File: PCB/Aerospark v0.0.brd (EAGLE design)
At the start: 59.1 x 42.9 mm, 34 parts, among them U1 TMP102

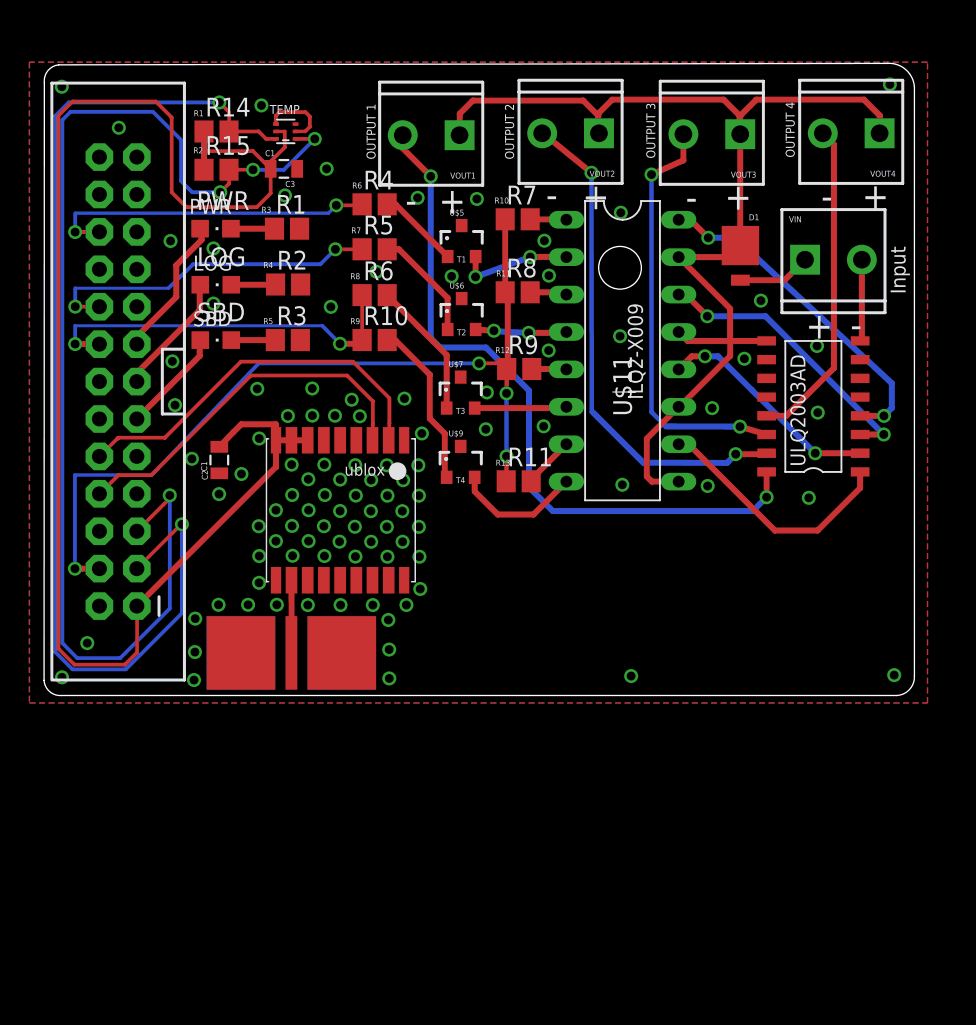
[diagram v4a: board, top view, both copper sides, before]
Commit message: Updated PCB and added mounting hole
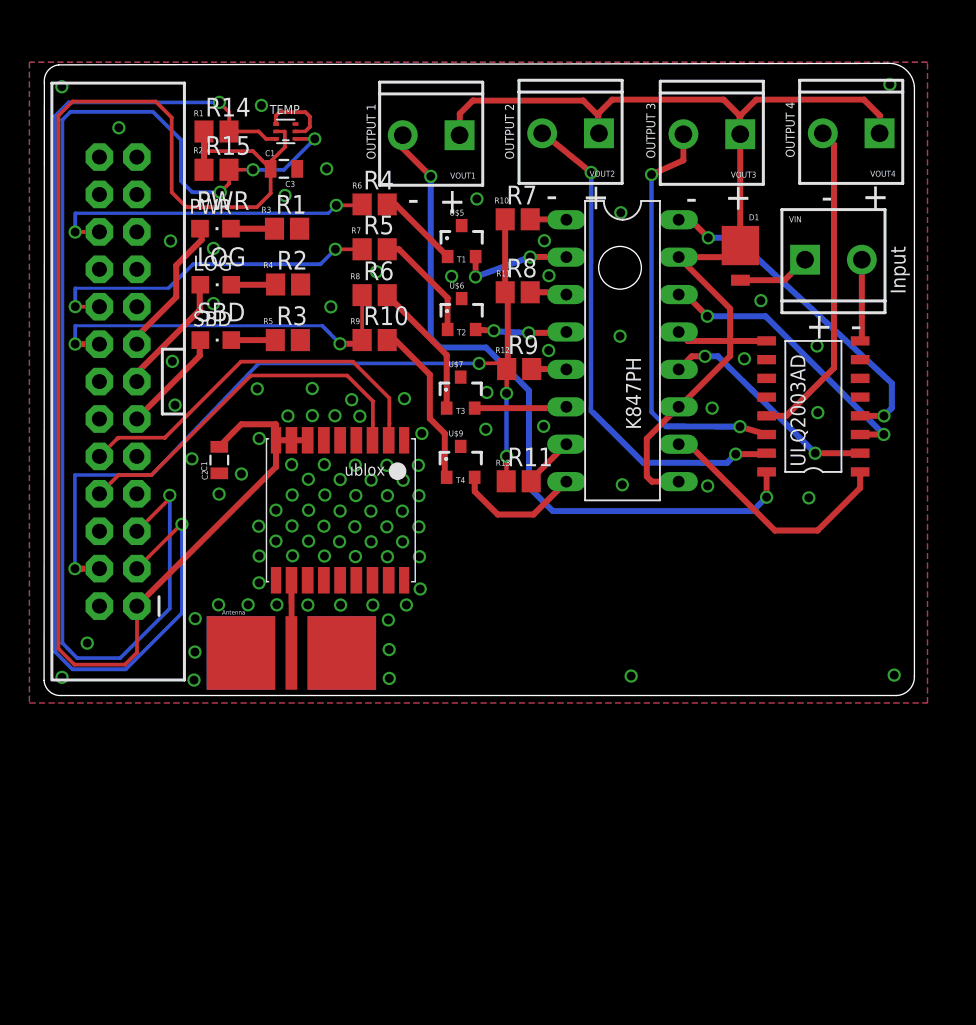
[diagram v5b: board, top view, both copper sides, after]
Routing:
- net GND: vias 100 -> 99
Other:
- board text added: "Antenna"
- board text added: "K847PH"
- board text removed: "ILQ2-X009"
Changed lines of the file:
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@@
 <text x="54.452521875" y="24.800559375" size="1.778" layer="21">-</text>
 <text x="58.2041" y="27.75711875" size="1.016" layer="21" rot="R90">Input</text>
-<text x="40.371021875" y="20.590040625" size="1.016" layer="21" rot="R90">ILQ2-X009</text>
 <text x="51.4030625" y="16.051078125" size="1.016" layer="21" rot="R90">ULQ2003AD</text>
 <text x="9.580878125" y="33.207959375" size="1.016" layer="21">PWR</text>
@@
 <text x="30.3784" y="16.1036" size="0.4064" layer="21">R13</text>
 <text x="26.51251875" y="33.2257375" size="1.778" layer="21">+</text>
-<text x="24.2443" y="33.253678125" size="1.778" layer="21">-</text>
+<text x="24.392890625" y="33.38321875" size="1.778" layer="21">-</text>
 <hole x="38.81818125" y="29.542159375" drill="2.9"/>
+<text x="40.24121875" y="18.5547" size="1.016" layer="21" rot="R90">K847PH</text>
+<text x="11.80338125" y="6.00075" size="0.3048" layer="21">Antenna</text>
 </plain>
 <attributes>
@@
 </class>
 </classes>
-<designrules name="OSHPark">
-<description language="de">&lt;b&gt;EAGLE Design Rules&lt;/b&gt;
+<designrules name="Hackvana">
+<description language="de">&lt;b&gt;EAGLE Design Rules für Hackvana&lt;/b&gt;
 &lt;p&gt;
 Die Standard-Design-Rules sind so gewählt, dass sie für
@@
 Einstellungen hier und speichern die Design Rules unter
 einem neuen Namen ab.</description>
-<description language="en">&lt;b&gt;Laen's PCB Order Design Rules&lt;/b&gt;
+<description language="en">&lt;b&gt;EAGLE Design Rules for Hackvana&lt;/b&gt;
 &lt;p&gt;
-Please make sure your boards conform to these design rules.</description>
+The default Design Rules have been set to cover
+a wide range of applications. Your particular design
+may have different requirements, so please make the
+necessary adjustments and save your customized
+design rules under a new name.</description>
+<description language="zh">&lt;b&gt;EAGLE Design Rules for Hackvana&lt;/b&gt;
+</description>
 <param name="layerSetup" value="(1*16)"/>
-<param name="mtCopper" value="0.0356mm 0.0356mm 0.0356mm 0.0356mm 0.0356mm 0.0356mm 0.0356mm 0.0356mm 0.0356mm 0.0356mm 0.0356mm 0.0356mm 0.0356mm 0.0356mm 0.0356mm 0.0356mm"/>
-<param name="mtIsolate" value="1.5011mm 0.1499mm 0.2007mm 0.1499mm 0.2007mm 0.1499mm 0.2007mm 0.1499mm 0.2007mm 0.1499mm 0.2007mm 0.1499mm 0.2007mm 0.1499mm 0.2007mm"/>
+<param name="mtCopper" value="0.035mm 0.035mm 0.035mm 0.035mm 0.035mm 0.035mm 0.035mm 0.035mm 0.035mm 0.035mm 0.035mm 0.035mm 0.035mm 0.035mm 0.035mm 0.035mm"/>
+<param name="mtIsolate" value="1.5mm 0.15mm 0.2mm 0.15mm 0.2mm 0.15mm 0.2mm 0.15mm 0.2mm 0.15mm 0.2mm 0.15mm 0.2mm 0.15mm 0.2mm"/>
 <param name="mdWireWire" value="6mil"/>
 <param name="mdWirePad" value="6mil"/>
@@
 <param name="mdPadVia" value="6mil"/>
 <param name="mdViaVia" value="6mil"/>
-<param name="mdSmdPad" value="6mil"/>
-<param name="mdSmdVia" value="6mil"/>
-<param name="mdSmdSmd" value="6mil"/>
+<param name="mdSmdPad" value="0mil"/>
+<param name="mdSmdVia" value="0mil"/>
+<param name="mdSmdSmd" value="0mil"/>
 <param name="mdViaViaSameLayer" value="8mil"/>
 <param name="mnLayersViaInSmd" value="2"/>
-<param name="mdCopperDimension" value="15mil"/>
+<param name="mdCopperDimension" value="6mil"/>
 <param name="mdDrill" value="6mil"/>
 <param name="mdSmdStop" value="0mil"/>
 <param name="msWidth" value="6mil"/>
-<param name="msDrill" value="13mil"/>
-<param name="msMicroVia" value="13mil"/>
+<param name="msDrill" value="0.3mm"/>
+<param name="msMicroVia" value="0.25mm"/>
 <param name="msBlindViaRatio" value="0.5"/>
 <param name="rvPadTop" value="0.25"/>
@@
 <param name="rvMicroViaOuter" value="0.25"/>
 <param name="rvMicroViaInner" value="0.25"/>
-<param name="rlMinPadTop" value="7mil"/>
+<param name="rlMinPadTop" value="10mil"/>
 <param name="rlMaxPadTop" value="20mil"/>
-<param name="rlMinPadInner" value="7mil"/>
+<param name="rlMinPadInner" value="10mil"/>
 <param name="rlMaxPadInner" value="20mil"/>
-<param name="rlMinPadBottom" value="7mil"/>
+<param name="rlMinPadBottom" value="10mil"/>
 <param name="rlMaxPadBottom" value="20mil"/>
-<param name="rlMinViaOuter" value="7mil"/>
+<param name="rlMinViaOuter" value="6mil"/>
 <param name="rlMaxViaOuter" value="20mil"/>
-<param name="rlMinViaInner" value="7mil"/>
+<param name="rlMinViaInner" value="6mil"/>
 <param name="rlMaxViaInner" value="20mil"/>
 <param name="rlMinMicroViaOuter" value="4mil"/>
@@
 <param name="psTop" value="-1"/>
 <param name="psBottom" value="-1"/>
-<param name="psFirst" value="-1"/>
+<param name="psFirst" value="0"/>
 <param name="psElongationLong" value="100"/>
 <param name="psElongationOffset" value="100"/>
 <param name="mvStopFrame" value="1"/>
 <param name="mvCreamFrame" value="0"/>
-<param name="mlMinStopFrame" value="3mil"/>
-<param name="mlMaxStopFrame" value="3mil"/>
+<param name="mlMinStopFrame" value="2mil"/>
+<param name="mlMaxStopFrame" value="2mil"/>
 <param name="mlMinCreamFrame" value="0mil"/>
 <param name="mlMaxCreamFrame" value="0mil"/>
-<param name="mlViaStopLimit" value="0mil"/>
+<param name="mlViaStopLimit" value="100mil"/>
 <param name="srRoundness" value="0"/>
 <param name="srMinRoundness" value="0mil"/>
@@
 <param name="checkAngle" value="0"/>
 <param name="checkFont" value="1"/>
-<param name="checkRestrict" value="1"/>
+<param name="checkRestrict" value="0"/>
 <param name="useDiameter" value="13"/>
 <param name="maxErrors" value="50"/>
@@
 <via x="33.99366875" y="29.00988125" extent="1-16" drill="0.6"/>
 <via x="22.2885" y="29.2735" extent="1-16" drill="0.6"/>
-<via x="25.0825" y="34.29" extent="1-16" drill="0.6"/>
+<wire x1="25.77591875" y1="33.7413625" x2="25.77591875" y2="33.7413625" width="0" layer="19" extent="1-16"/>
 <via x="29.7815" y="21.082" extent="1-16" drill="0.6"/>
 <via x="27.388" y="28.96" extent="1-16" drill="0.6"/>
@@
 <contactref element="VOUT2" pad="2"/>
 <wire x1="33.5332" y1="38.6715" x2="33.5915" y2="38.6715" width="0.4064" layer="1"/>
-<wire x1="33.5915" y1="38.6715" x2="36.8782625" y2="35.99381875" width="0.4064" layer="1"/>
-<via x="36.8782625" y="35.99381875" extent="1-16" drill="0.6"/>
+<wire x1="33.5915" y1="38.6715" x2="36.8592125" y2="36.01286875" width="0.4064" layer="1"/>
+<via x="36.8592125" y="36.01286875" extent="1-16" drill="0.6"/>
 <via x="46.6725" y="16.891" extent="1-16" drill="0.6"/>
 <wire x1="46.6725" y1="16.891" x2="48.7045" y2="16.891" width="0.4064" layer="1"/>
@@
 <wire x1="40.400303125" y1="16.3112375" x2="46.0775" y2="16.296" width="0.4064" layer="16"/>
 <wire x1="46.0775" y1="16.296" x2="46.6725" y2="16.891" width="0.4064" layer="16"/>
-<wire x1="36.8782625" y1="35.99381875" x2="36.899853125" y2="19.7521625" width="0.3048" layer="16"/>
-<wire x1="36.899853125" y1="19.7521625" x2="36.989940625" y2="19.71525" width="0.3048" layer="16"/>
+<wire x1="36.8592125" y1="36.01286875" x2="36.842703125" y2="19.7902625" width="0.3048" layer="16"/>
+<wire x1="36.842703125" y1="19.7902625" x2="36.989940625" y2="19.71525" width="0.3048" layer="16"/>
 </signal>
 <signal name="N$21">
